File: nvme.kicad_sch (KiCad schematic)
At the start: 1 part, among them J3 pcie_m2_ngff

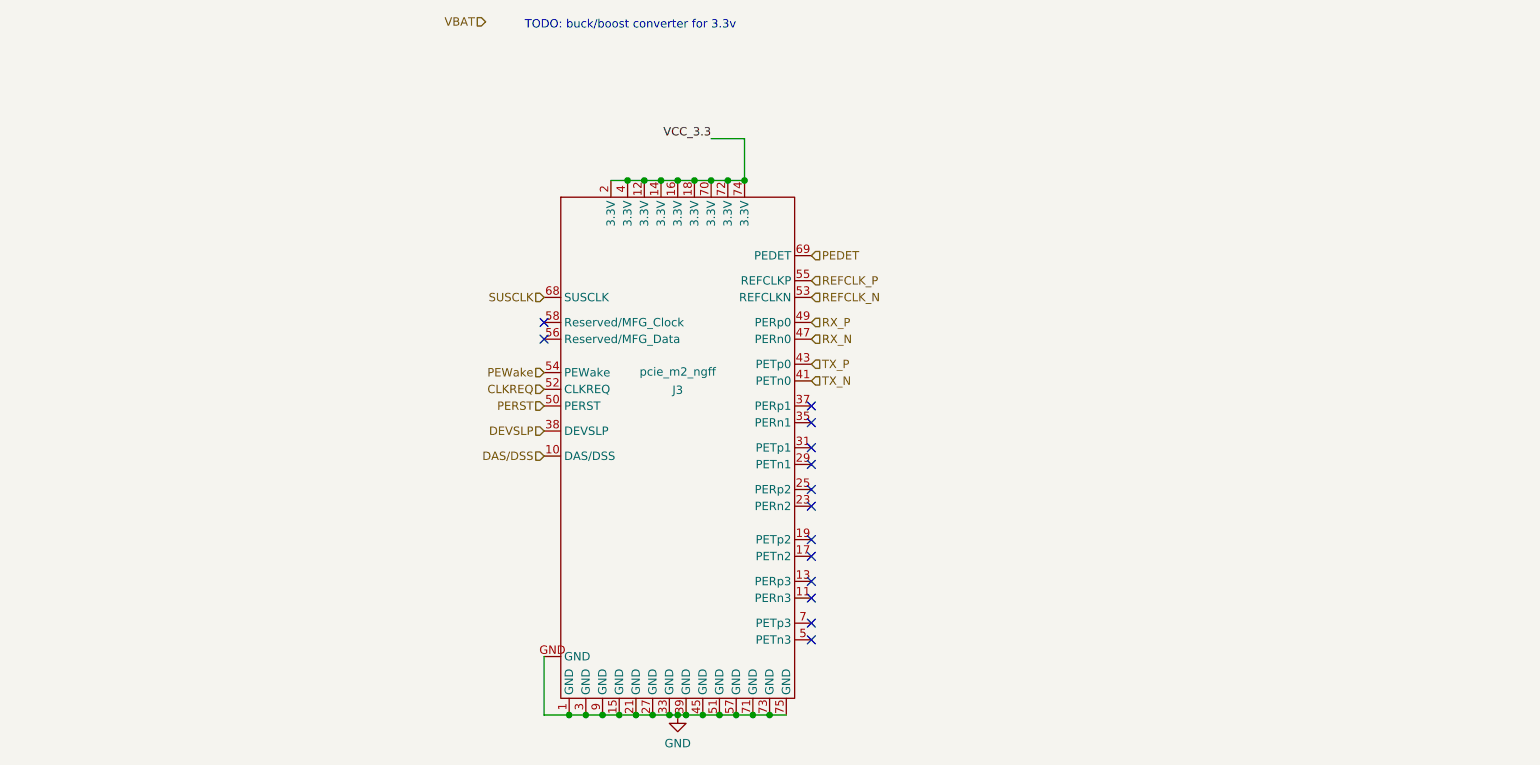
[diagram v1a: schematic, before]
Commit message: Add buck-boost regulator for PCIe 3.3V
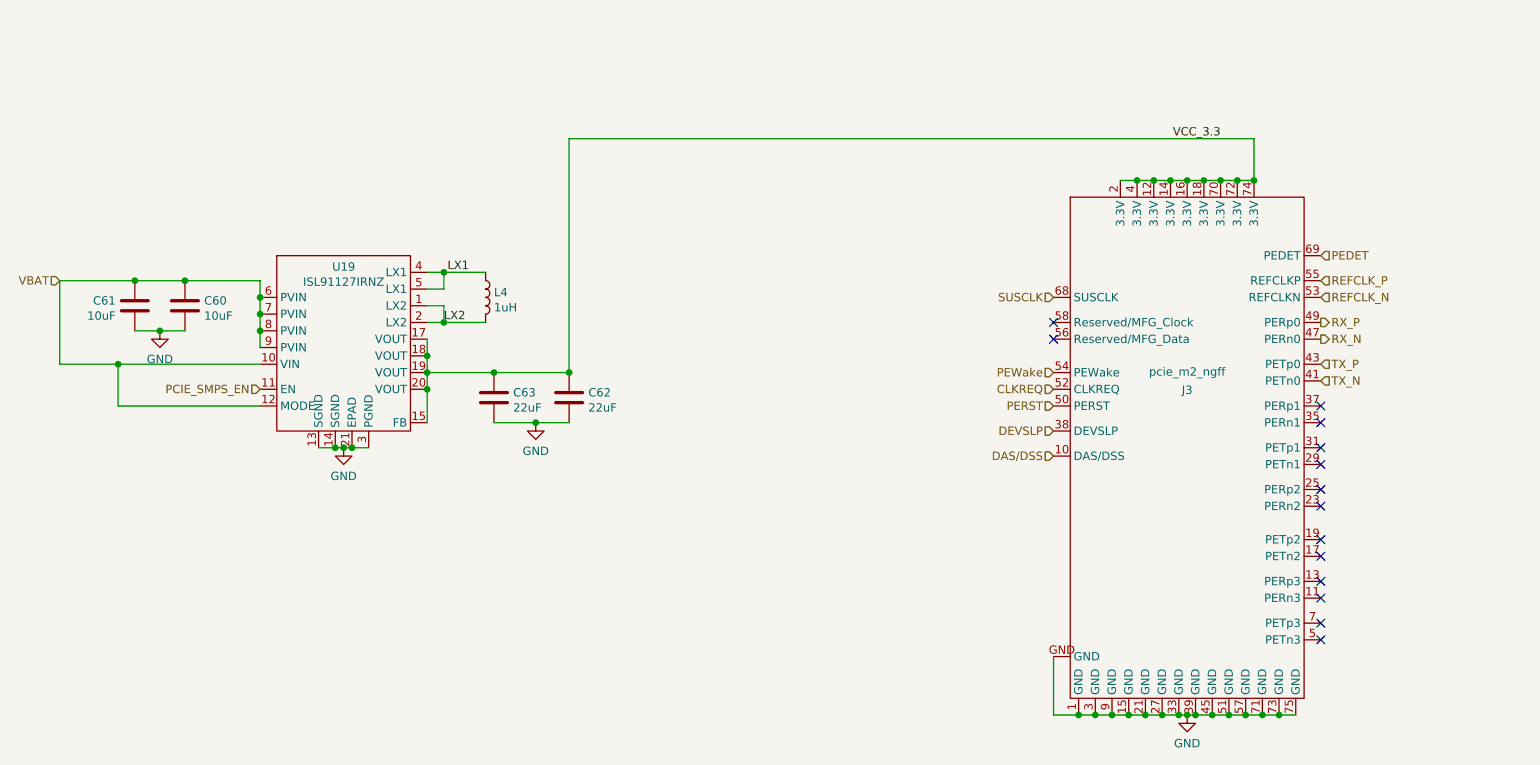
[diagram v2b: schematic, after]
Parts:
- added C60, C61: 10uF, Capacitor_SMD:C_0402_1005Metric, symbol Device:C
- added C62, C63: 22uF, Capacitor_SMD:C_0805_2012Metric, symbol Device:C
- added L4: 1uH, Inductor_SMD:L_1008_2520Metric, symbol Device:L
- added U19: ISL91127IRNZ, Package_DFN_QFN:QFN-20-1EP_4x4mm_P0.5mm_EP2.7x2.7mm, symbol ISL91127IRNZ:ISL91127IRNZ
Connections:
- net GND: now also C60.2, C61.1, C62.2, C63.2, U19.13 (SGND), U19.14 (SGND), U19.21 (EPAD), U19.3 (PGND)
- net VBAT: now also C60.1, C61.2, U19.10 (VIN), U19.12 (MODE), U19.6 (PVIN), U19.7 (PVIN), U19.8 (PVIN), U19.9 (PVIN)
- net VCC_3.3: now also C62.1, C63.1, U19.15 (FB), U19.17 (VOUT), U19.18 (VOUT), U19.19 (VOUT), U19.20 (VOUT)
- new net LX1: L4.1, U19.4 (LX1), U19.5 (LX1)
- new net LX2: L4.2, U19.1 (LX2), U19.2 (LX2)
- new net PCIE_SMPS_EN: U19.11 (EN)
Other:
- note removed: "TODO: buck/boost converter for 3.3v"
- moved on the sheet: J3

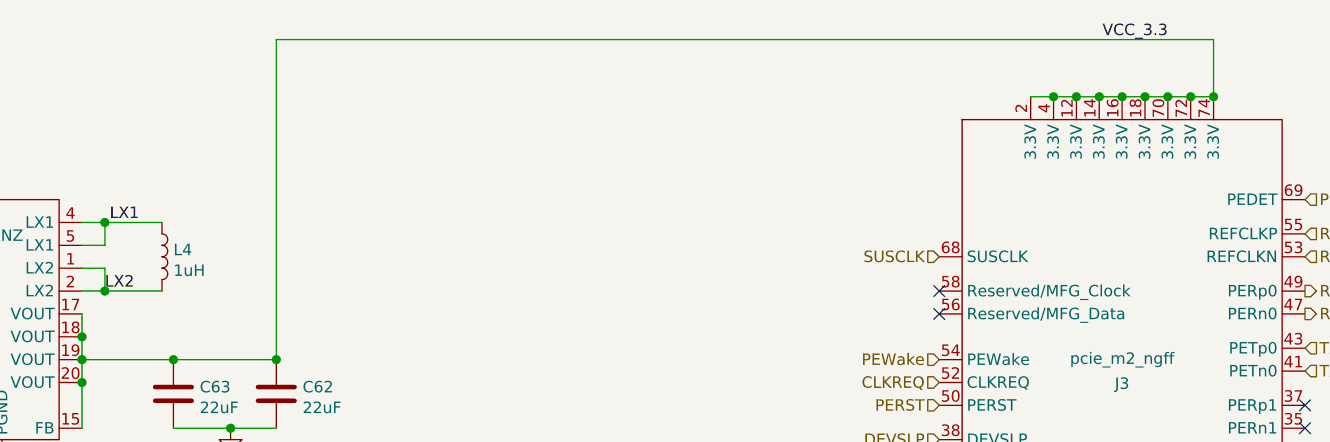
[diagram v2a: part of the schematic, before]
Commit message: Route CM4 board with differential connector on the right.
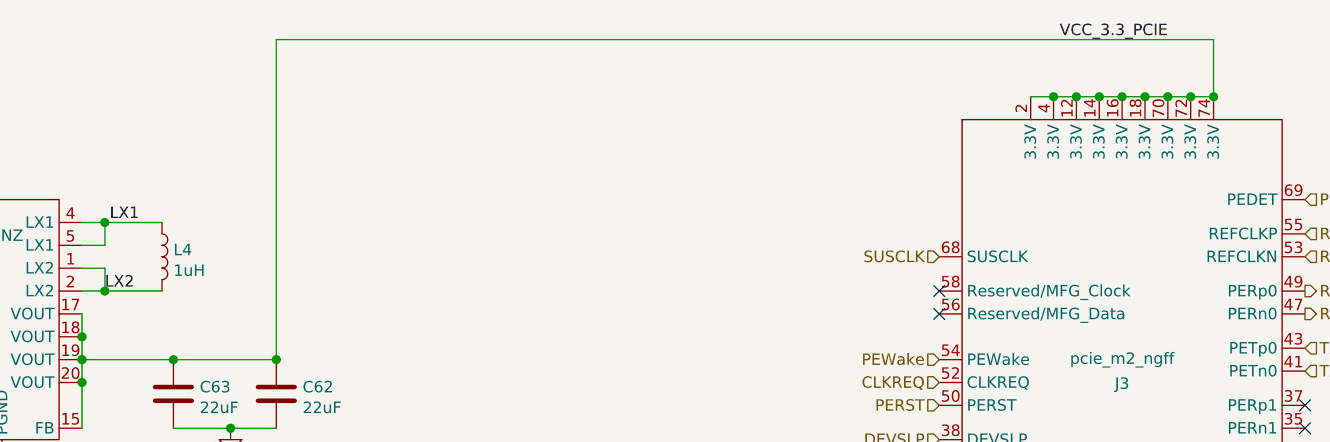
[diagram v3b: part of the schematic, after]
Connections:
- net VCC_3.3 renamed VCC_3.3_PCIE

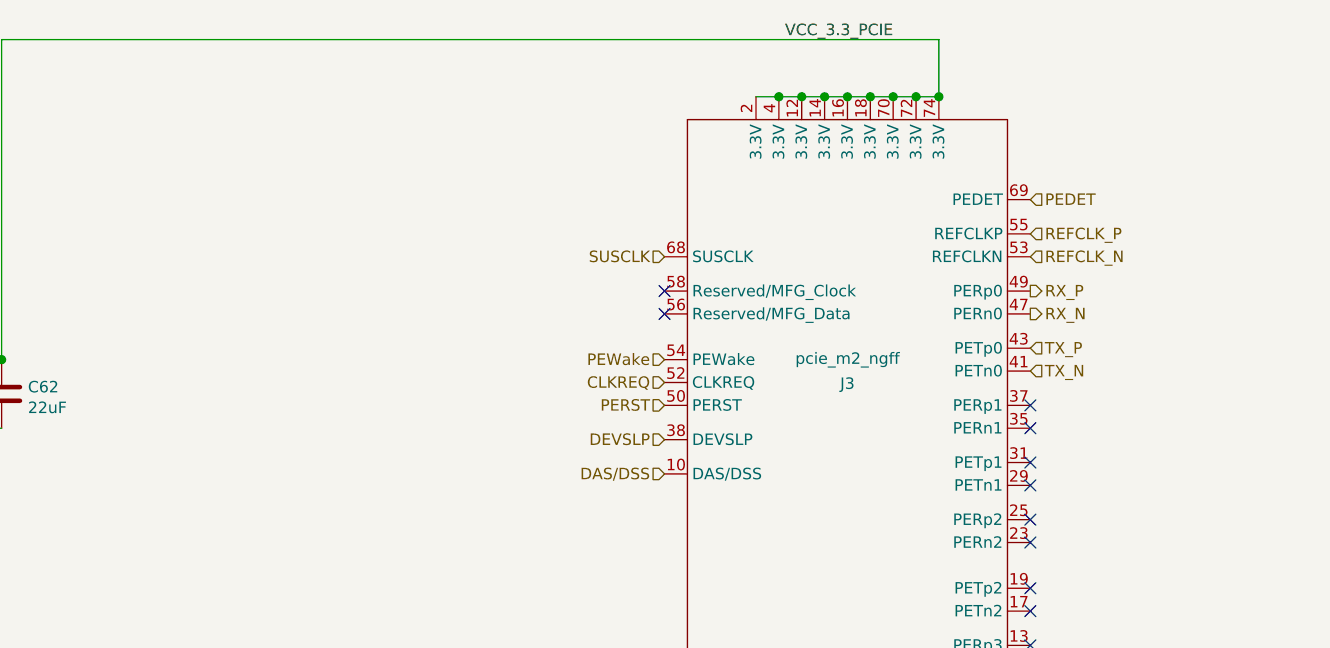
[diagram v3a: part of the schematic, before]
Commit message: Lots of tiny test points; add 3d models to a bunch of things. Re-length-match PCIe and DSI traces.
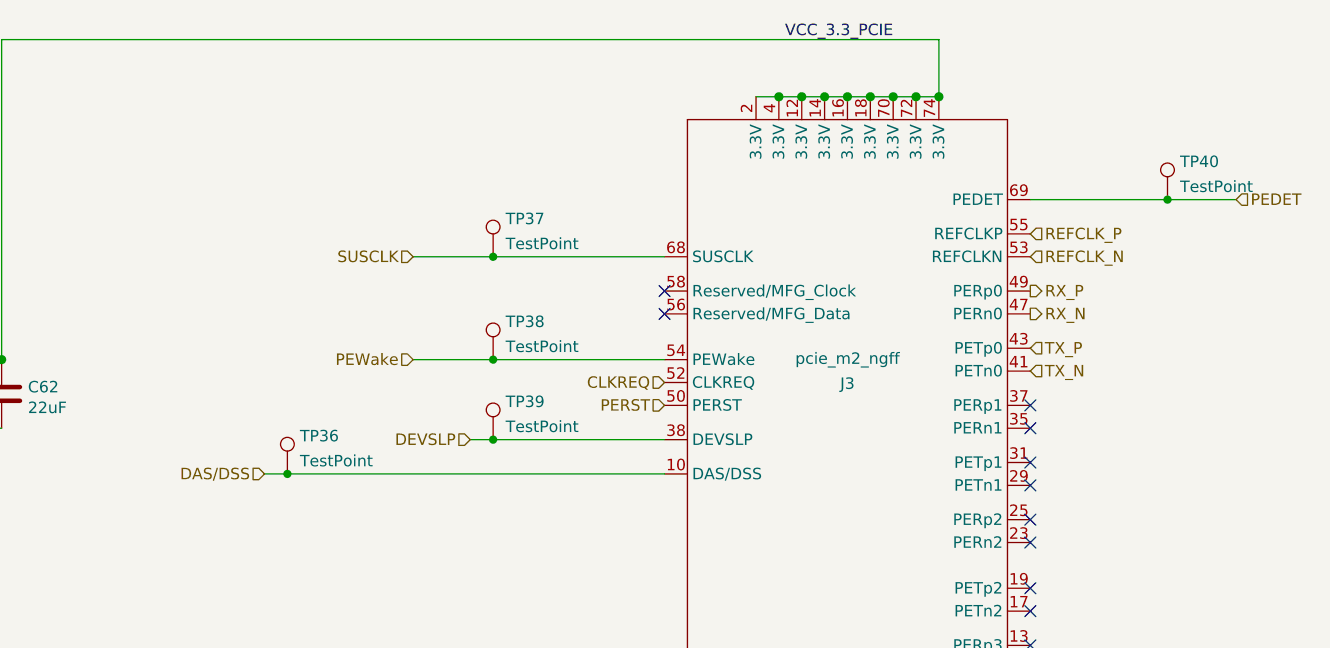
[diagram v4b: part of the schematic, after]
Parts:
- added TP36, TP37, TP38, TP39, TP40: TestPoint, footprints:testpoint_small, symbol Connector:TestPoint
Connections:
- net DAS/DSS: now also TP36.1
- net DEVSLP: now also TP39.1
- net PEDET: now also TP40.1
- net PEWake: now also TP38.1
- net SUSCLK: now also TP37.1
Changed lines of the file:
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@@
   (junction (at 91.44 97.79) (diameter 1.016) (color 0 0 0 0)
   )
+  (junction (at 254 68.58) (diameter 0) (color 0 0 0 0)
+  )
   (junction (at 119.38 93.98) (diameter 1.016) (color 0 0 0 0)
   )
@@
   (junction (at 105.41 78.74) (diameter 1.016) (color 0 0 0 0)
   )
+  (junction (at 156.21 99.06) (diameter 0) (color 0 0 0 0)
+  )
+  (junction (at 179.07 86.36) (diameter 0) (color 0 0 0 0)
+  )
   (junction (at 88.9 97.79) (diameter 1.016) (color 0 0 0 0)
   )
   (junction (at 218.44 138.43) (diameter 1.016) (color 0 0 0 0)
   )
+  (junction (at 179.07 74.93) (diameter 0) (color 0 0 0 0)
+  )
   (junction (at 214.63 138.43) (diameter 1.016) (color 0 0 0 0)
   )
@@
   )
   (junction (at 55.88 85.09) (diameter 1.016) (color 0 0 0 0)
+  )
+  (junction (at 179.07 95.25) (diameter 0) (color 0 0 0 0)
   )
   (junction (at 90.17 97.79) (diameter 1.016) (color 0 0 0 0)
@@
   (no_connect (at 198.12 78.74))
   (no_connect (at 198.12 81.28))
+  (wire (pts (xy 170.18 86.36) (xy 179.07 86.36))
+    (stroke (width 0) (type default) (color 0 0 0 0))
+  )
   (wire (pts (xy 102.87 71.12) (xy 105.41 71.12))
     (stroke (width 0) (type solid) (color 0 0 0 0))
@@
     (stroke (width 0) (type solid) (color 0 0 0 0))
   )
+  (wire (pts (xy 179.07 74.93) (xy 198.12 74.93))
+    (stroke (width 0) (type default) (color 0 0 0 0))
+  )
   (wire (pts (xy 113.03 93.98) (xy 119.38 93.98))
     (stroke (width 0) (type solid) (color 0 0 0 0))
@@
     (stroke (width 0) (type solid) (color 0 0 0 0))
   )
+  (wire (pts (xy 179.07 86.36) (xy 198.12 86.36))
+    (stroke (width 0) (type default) (color 0 0 0 0))
+  )
   (wire (pts (xy 124.46 86.36) (xy 124.46 50.8))
     (stroke (width 0) (type solid) (color 0 0 0 0))
@@
     (stroke (width 0) (type solid) (color 0 0 0 0))
   )
+  (wire (pts (xy 153.67 99.06) (xy 156.21 99.06))
+    (stroke (width 0) (type default) (color 0 0 0 0))
+  )
+  (wire (pts (xy 176.53 95.25) (xy 179.07 95.25))
+    (stroke (width 0) (type default) (color 0 0 0 0))
+  )
   (wire (pts (xy 86.36 97.79) (xy 88.9 97.79))
     (stroke (width 0) (type solid) (color 0 0 0 0))
@@
     (stroke (width 0) (type solid) (color 0 0 0 0))
   )
+  (wire (pts (xy 261.62 68.58) (xy 254 68.58))
+    (stroke (width 0) (type default) (color 0 0 0 0))
+  )
   (wire (pts (xy 55.88 85.09) (xy 55.88 91.44))
     (stroke (width 0) (type solid) (color 0 0 0 0))
@@
     (stroke (width 0) (type solid) (color 0 0 0 0))
   )
+  (wire (pts (xy 170.18 74.93) (xy 179.07 74.93))
+    (stroke (width 0) (type default) (color 0 0 0 0))
+  )
   (wire (pts (xy 209.55 138.43) (xy 212.09 138.43))
     (stroke (width 0) (type solid) (color 0 0 0 0))
@@
     (stroke (width 0) (type solid) (color 0 0 0 0))
   )
+  (wire (pts (xy 254 68.58) (xy 238.76 68.58))
+    (stroke (width 0) (type default) (color 0 0 0 0))
+  )
   (wire (pts (xy 113.03 86.36) (xy 124.46 86.36))
     (stroke (width 0) (type solid) (color 0 0 0 0))
+  )
+  (wire (pts (xy 179.07 95.25) (xy 198.12 95.25))
+    (stroke (width 0) (type default) (color 0 0 0 0))
+  )
+  (wire (pts (xy 156.21 99.06) (xy 198.12 99.06))
+    (stroke (width 0) (type default) (color 0 0 0 0))
   )
   (wire (pts (xy 58.42 72.39) (xy 66.04 72.39))
@@
     (effects (font (size 1.27 1.27)) (justify right))
   )
-  (hierarchical_label "DEVSLP" (shape input) (at 198.12 95.25 180)
+  (hierarchical_label "DEVSLP" (shape input) (at 176.53 95.25 180)
     (effects (font (size 1.27 1.27)) (justify right))
   )
@@
     (effects (font (size 1.27 1.27)) (justify left))
   )
-  (hierarchical_label "PEWake" (shape input) (at 198.12 86.36 180)
-    (effects (font (size 1.27 1.27)) (justify right))
-  )
-  (hierarchical_label "DAS{slash}DSS" (shape input) (at 198.12 99.06 180)
-    (effects (font (size 1.27 1.27)) (justify right))
-  )
-  (hierarchical_label "SUSCLK" (shape input) (at 198.12 74.93 180)
+  (hierarchical_label "PEWake" (shape input) (at 170.18 86.36 180)
+    (effects (font (size 1.27 1.27)) (justify right))
+  )
+  (hierarchical_label "DAS{slash}DSS" (shape input) (at 153.67 99.06 180)
+    (effects (font (size 1.27 1.27)) (justify right))
+  )
+  (hierarchical_label "SUSCLK" (shape input) (at 170.18 74.93 180)
     (effects (font (size 1.27 1.27)) (justify right))
   )
@@
     (effects (font (size 1.27 1.27)) (justify left))
   )
-  (hierarchical_label "PEDET" (shape input) (at 238.76 68.58 0)
+  (hierarchical_label "PEDET" (shape input) (at 261.62 68.58 0)
     (effects (font (size 1.27 1.27)) (justify left))
   )
@@
     (pin "2")
   )
+  (symbol (lib_id "Connector:TestPoint") (at 254 68.58 0) (unit 1)
+    (in_bom yes) (on_board yes) (fields_autoplaced)
+    (property "Reference" "TP40" (id 0) (at 255.397 64.3695 0)
+      (effects (font (size 1.27 1.27)) (justify left))
+    )
+    (property "Value" "TestPoint" (id 1) (at 255.397 67.1446 0)
+      (effects (font (size 1.27 1.27)) (justify left))
+    )
+    (property "Footprint" "footprints:testpoint_small" (id 2) (at 259.08 68.58 0)
+      (effects (font (size 1.27 1.27)) hide)
+    )
+    (property "Datasheet" "~" (id 3) (at 259.08 68.58 0)
+      (effects (font (size 1.27 1.27)) hide)
+    )
+    (pin "1")
+  )
   (symbol (lib_id "Device:C") (at 58.42 76.2 0) (mirror x) (unit 1)
     (in_bom yes) (on_board yes) (fields_autoplaced)
@@
       (effects (font (size 1.27 1.27)) hide)
     )
+    (pin "1")
+  )
+  (symbol (lib_id "Connector:TestPoint") (at 156.21 99.06 0) (unit 1)
+    (in_bom yes) (on_board yes) (fields_autoplaced)
+    (property "Reference" "TP36" (id 0) (at 157.607 94.8495 0)
+      (effects (font (size 1.27 1.27)) (justify left))
+    )
+    (property "Value" "TestPoint" (id 1) (at 157.607 97.6246 0)
+      (effects (font (size 1.27 1.27)) (justify left))
+    )
+    (property "Footprint" "footprints:testpoint_small" (id 2) (at 161.29 99.06 0)
+      (effects (font (size 1.27 1.27)) hide)
+    )
+    (property "Datasheet" "~" (id 3) (at 161.29 99.06 0)
+      (effects (font (size 1.27 1.27)) hide)
+    )
+    (pin "1")
+  )
+  (symbol (lib_id "Connector:TestPoint") (at 179.07 95.25 0) (unit 1)
+    (in_bom yes) (on_board yes) (fields_autoplaced)
+    (property "Reference" "TP39" (id 0) (at 180.467 91.0395 0)
+      (effects (font (size 1.27 1.27)) (justify left))
+    )
+    (property "Value" "TestPoint" (id 1) (at 180.467 93.8146 0)
+      (effects (font (size 1.27 1.27)) (justify left))
+    )
+    (property "Footprint" "footprints:testpoint_small" (id 2) (at 184.15 95.25 0)
+      (effects (font (size 1.27 1.27)) hide)
+    )
+    (property "Datasheet" "~" (id 3) (at 184.15 95.25 0)
+      (effects (font (size 1.27 1.27)) hide)
+    )
+    (pin "1")
+  )
+  (symbol (lib_id "Connector:TestPoint") (at 179.07 74.93 0) (unit 1)
+    (in_bom yes) (on_board yes) (fields_autoplaced)
+    (property "Reference" "TP37" (id 0) (at 180.467 70.7195 0)
+      (effects (font (size 1.27 1.27)) (justify left))
+    )
+    (property "Value" "TestPoint" (id 1) (at 180.467 73.4946 0)
+      (effects (font (size 1.27 1.27)) (justify left))
+    )
+    (property "Footprint" "footprints:testpoint_small" (id 2) (at 184.15 74.93 0)
+      (effects (font (size 1.27 1.27)) hide)
+    )
+    (property "Datasheet" "~" (id 3) (at 184.15 74.93 0)
+      (effects (font (size 1.27 1.27)) hide)
+    )
+    (pin "1")
+  )
+  (symbol (lib_id "Connector:TestPoint") (at 179.07 86.36 0) (unit 1)
+    (in_bom yes) (on_board yes) (fields_autoplaced)
+    (property "Reference" "TP38" (id 0) (at 180.467 82.1495 0)
+      (effects (font (size 1.27 1.27)) (justify left))
+    )
+    (property "Value" "TestPoint" (id 1) (at 180.467 84.9246 0)
+      (effects (font (size 1.27 1.27)) (justify left))
+    )
+    (property "Footprint" "footprints:testpoint_small" (id 2) (at 184.15 86.36 0)
+      (effects (font (size 1.27 1.27)) hide)
+    )
+    (property "Datasheet" "~" (id 3) (at 184.15 86.36 0)
+      (effects (font (size 1.27 1.27)) hide)
+    )
